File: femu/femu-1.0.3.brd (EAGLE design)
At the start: 24.1 x 15.8 mm, 56 parts, among them IC1 ESP32-QFN_5X5

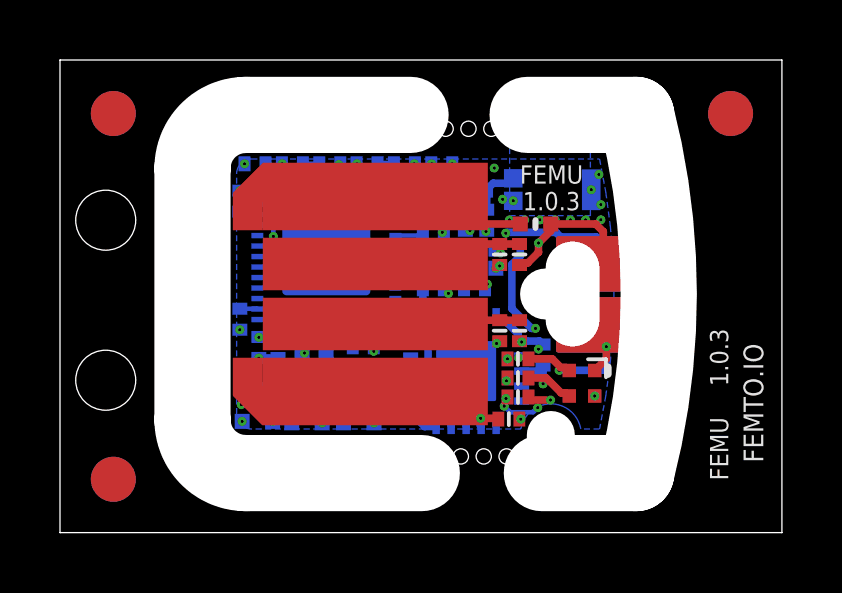
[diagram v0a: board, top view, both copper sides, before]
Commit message: Adjusting MPNs for FEMU 1.0.3
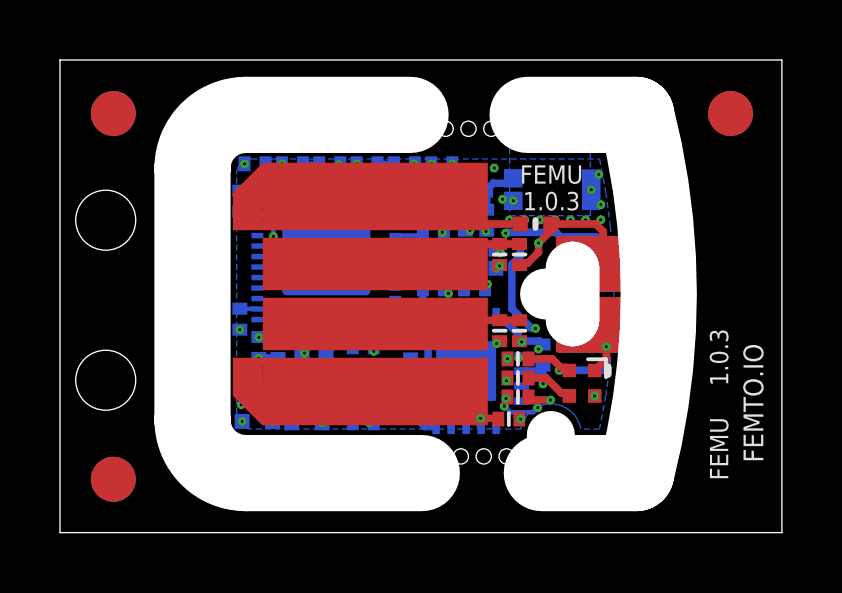
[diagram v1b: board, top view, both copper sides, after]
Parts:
- C23: device microbuilder:_0402MP -> parts_0201:PART
- C24: value 10nF -> 10nF/6.3V(10%)
- moved C23 0.15 mm to (10.1, 3.66)
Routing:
- net GND: track 70.1 -> 75.5 mm

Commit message: Adding current work on FEMU v1.0.3, which includes microvia adjustments
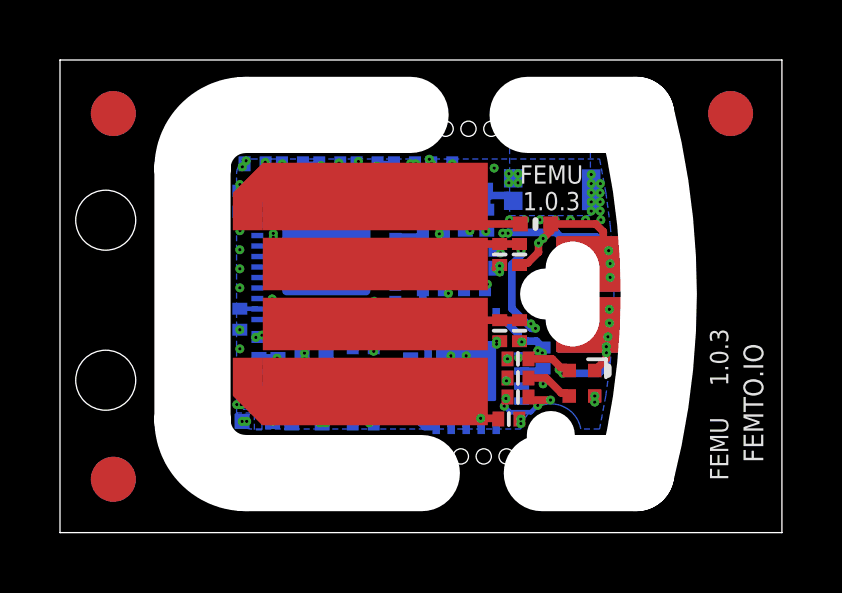
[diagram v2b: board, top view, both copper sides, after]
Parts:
- moved C25 0.10 mm to (16.1, 5.82)
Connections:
- net GND: now also ANT1.2; no longer ANT1.1
- net N$6: now also ANT1.1; no longer ANT1.2
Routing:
- net GND: track 75.5 -> 81.6 mm, vias 66 -> 100
- net 3.3V: track 51.7 -> 55.4 mm, vias 21 -> 33
- net IO26/DAC2: track 10.8 -> 12.3 mm, vias 4 -> 9
- net IO25/DAC1: track 10.5 -> 11.9 mm, vias 4 -> 9
- net N$3: track 2.73 -> 3.96 mm, vias 4 -> 6
- net N$14: track 5.35 -> 6.40 mm, vias 4 -> 6
- net VIN: track 16.3 -> 17.3 mm, vias 10 -> 13
- net N$7: track 4.71 -> 5.57 mm, vias 4 -> 6
- net IO27/R: track 19.6 -> 20.5 mm, vias 12 -> 16
- net USB+: track 2.15 -> 2.87 mm, vias 3 -> 5
- net XIN: track 7.49 -> 8.16 mm, vias 4 -> 6
- net N$9: track 6.65 -> 7.15 mm, vias 4 -> 6
- net IO4/G: track 11.6 -> 12.0 mm, vias 5 -> 6
- net USB-: track 1.52 -> 1.97 mm, vias 3 -> 5
- net TXD: track 12.0 -> 12.4 mm, vias 6 -> 8
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
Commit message: last updates to femu-1.0.3 committed
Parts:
- moved R5 0.10 mm to (15.3, 4.42)
- moved R4 0.05 mm to (15.3, 5.11)
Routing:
- net GND: track 81.6 -> 84.1 mm, vias 100 -> 101
